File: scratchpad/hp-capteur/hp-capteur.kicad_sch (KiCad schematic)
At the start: 19 parts, among them J1 vers XIAO ESP32-C3, U1 MCP6002

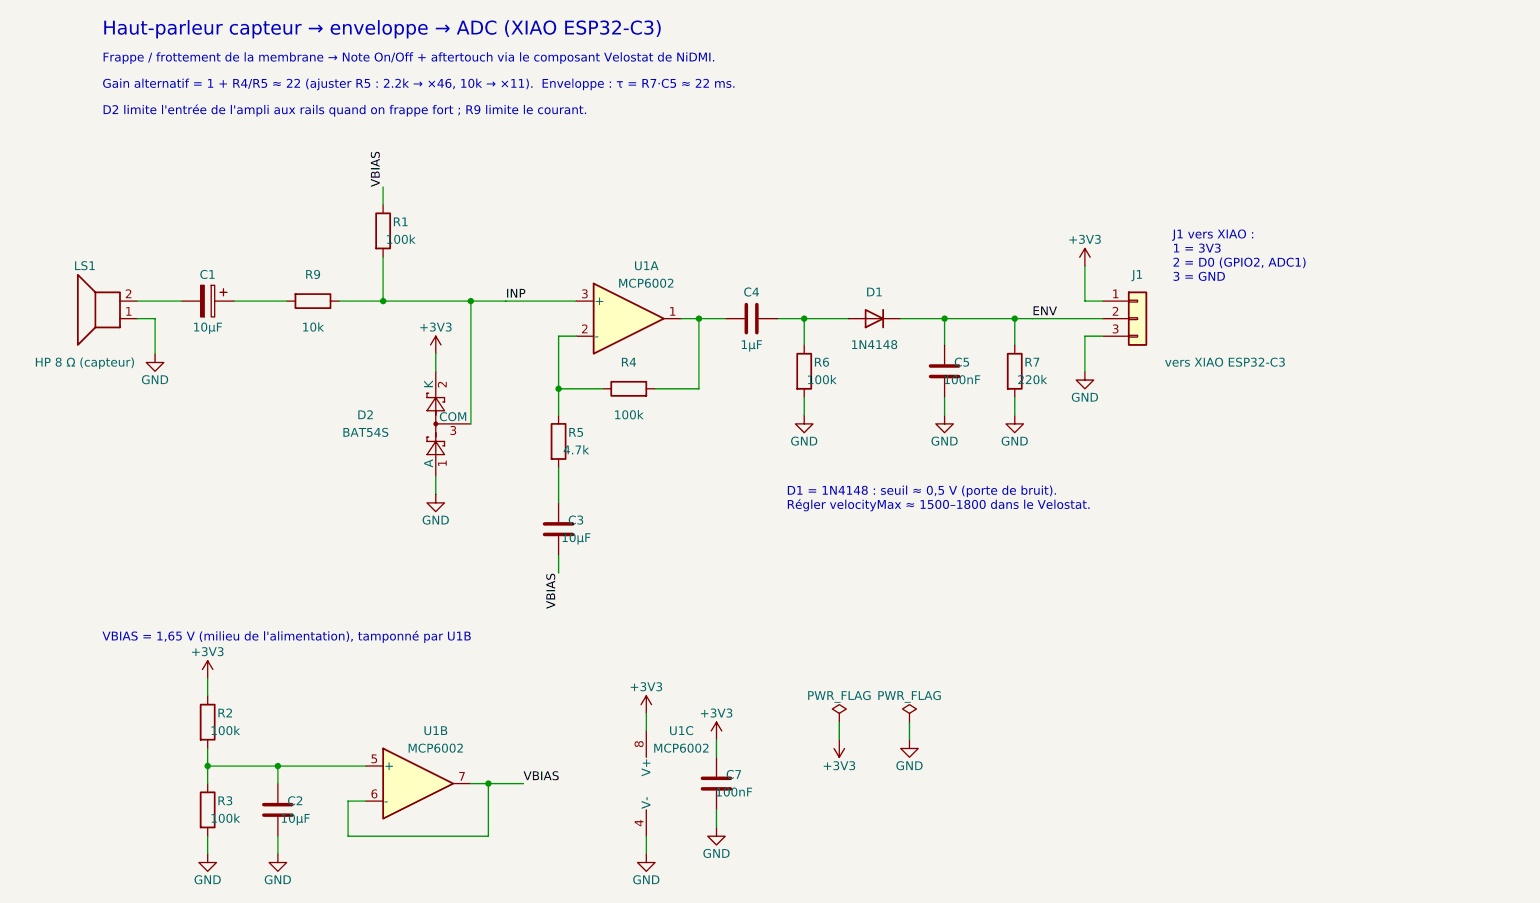
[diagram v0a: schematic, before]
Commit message: Schéma hp-capteur : clamp d'entrée en deux 1N4148 au lieu du BAT54S
D2 (INP → 3V3) et D3 (GND → INP) limitent l'entrée de l'ampli à
−0,6 V / +3,9 V ; R9 (10 k) limite le courant d'injection.

Co-Authored-By: Claude Opus 5.5 <noreply@anthropic.com>
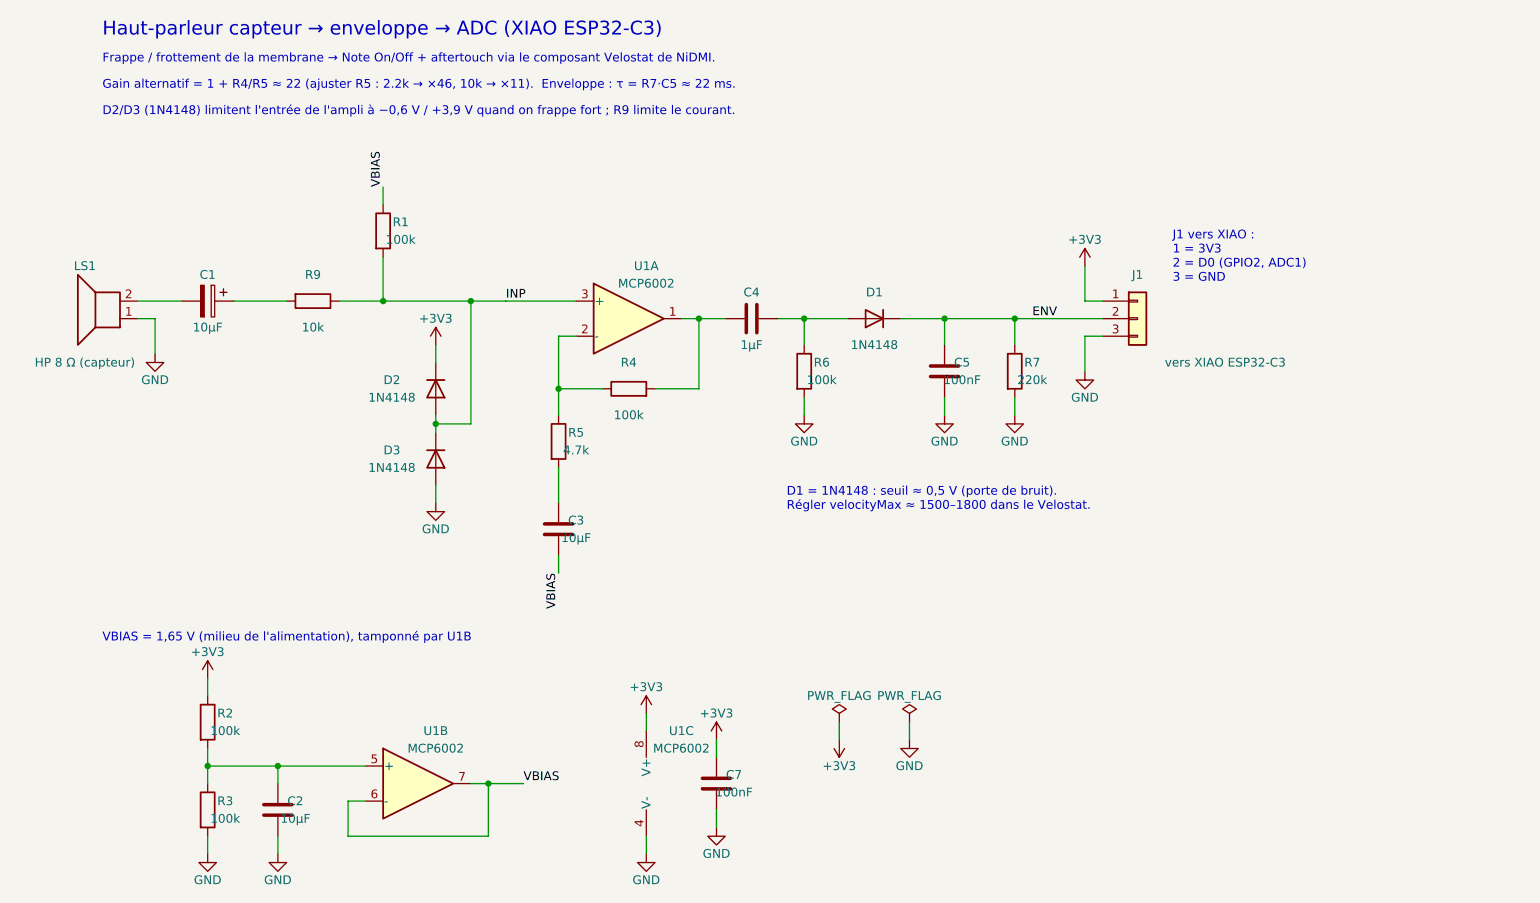
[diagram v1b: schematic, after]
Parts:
- added D3: 1N4148, symbol Diode:1N4148
- D2: value BAT54S -> 1N4148; symbol Diode:BAT54S -> Diode:1N4148
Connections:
- net +3V3: now also D2.1 (K); no longer D2.2 (K)
- net GND: now also D3.2 (A); no longer D2.1 (A)
- net INP: now also D2.2 (A), D3.1 (K); no longer D2.3 (COM)
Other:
- note added: "D2/D3 (1N4148) limitent l'entrée de l'ampli à −0,6 V / +3,9 V quand on frappe fort ; R9 limite le courant."
- note removed: "D2 limite l'entrée de l'ampli aux rails quand on frappe fort ; R9 limite le courant."
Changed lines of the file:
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@@
 	(wire
 		(pts
-			(xy 73.66 81.28)
-			(xy 73.66 83.82)
-		)
-		(stroke
-			(width 0)
-			(type default)
-		)
-	)
-	(wire
-		(pts
-			(xy 73.66 66.04)
-			(xy 73.66 63.5)
+			(xy 73.66 64.77)
+			(xy 73.66 62.23)
+		)
+		(stroke
+			(width 0)
+			(type default)
+		)
+	)
+	(wire
+		(pts
+			(xy 73.66 82.55)
+			(xy 73.66 85.09)
 		)
 		(stroke
@@
 			(xy 66.04 49.53)
 			(xy 66.04 55.88)
+		)
+		(stroke
+			(width 0)
+			(type default)
+		)
+	)
+	(wire
+		(pts
+			(xy 73.66 72.39)
+			(xy 73.66 73.66)
+		)
+		(stroke
+			(width 0)
+			(type default)
+		)
+	)
+	(wire
+		(pts
+			(xy 73.66 73.66)
+			(xy 73.66 74.93)
+		)
+		(stroke
+			(width 0)
+			(type default)
+		)
+	)
+	(wire
+		(pts
+			(xy 73.66 73.66)
+			(xy 78.74 73.66)
 		)
 		(stroke
@@
 	(junction
 		(at 78.74 55.88)
+		(diameter 0)
+		(color 0 0 0 0)
+	)
+	(junction
+		(at 73.66 73.66)
 		(diameter 0)
 		(color 0 0 0 0)
@@
 		)
 	)
-	(text "D2 limite l'entrée de l'ampli aux rails quand on frappe fort ; R9 limite le courant."
+	(text "D2/D3 (1N4148) limitent l'entrée de l'ampli à −0,6 V / +3,9 V quand on frappe fort ; R9 limite le courant."
 		(exclude_from_sim no)
 		(at 25.4 29.21 0)
@@
 	)
 	(symbol
-		(lib_id "Diode:BAT54S")
-		(at 73.66 73.66 90)
+		(lib_id "Diode:1N4148")
+		(at 73.66 68.58 270)
 		(unit 1)
 		(exclude_from_sim no)
@@
 		(dnp no)
 		(property "Reference" "D2"
-			(at 63.5 72.39 90)
-			(effects
-				(font
-					(size 1.27 1.27)
-				)
-			)
-		)
-		(property "Value" "BAT54S"
-			(at 63.5 74.93 90)
+			(at 67.31 67.31 90)
+			(effects
+				(font
+					(size 1.27 1.27)
+				)
+			)
+		)
+		(property "Value" "1N4148"
+			(at 67.31 69.85 90)
 			(effects
 				(font
@@
 		)
 		(property "Footprint" ""
-			(at 73.66 73.66 0)
+			(at 73.66 68.58 0)
 			(effects
 				(font
@@
 		)
 		(property "Datasheet" ""
-			(at 73.66 73.66 0)
+			(at 73.66 68.58 0)
 			(effects
 				(font
@@
 		)
 		(pin "1"
-		)
-		(pin "3"
 		)
 		(pin "2"
@@
 	)
 	(symbol
-		(lib_id "power:GND")
-		(at 73.66 83.82 0)
+		(lib_id "power:+3V3")
+		(at 73.66 62.23 0)
 		(unit 1)
 		(exclude_from_sim no)
@@
 		(dnp no)
 		(property "Reference" "#PWR001"
-			(at 73.66 83.82 0)
-			(effects
-				(font
-					(size 1.27 1.27)
-				)
-				(hide yes)
-			)
-		)
-		(property "Value" "GND"
-			(at 73.66 87.63 0)
+			(at 73.66 62.23 0)
+			(effects
+				(font
+					(size 1.27 1.27)
+				)
+				(hide yes)
+			)
+		)
+		(property "Value" "+3V3"
+			(at 73.66 58.42 0)
 			(effects
 				(font
@@
 		)
 		(property "Footprint" ""
-			(at 73.66 83.82 0)
+			(at 73.66 62.23 0)
 			(effects
 				(font
@@
 		)
 		(property "Datasheet" ""
-			(at 73.66 83.82 0)
+			(at 73.66 62.23 0)
 			(effects
 				(font
@@
 	)
 	(symbol
-		(lib_id "power:+3V3")
-		(at 73.66 63.5 0)
+		(lib_id "Diode:1N4148")
+		(at 73.66 78.74 270)
+		(unit 1)
+		(exclude_from_sim no)
+		(in_bom yes)
+		(on_board yes)
+		(dnp no)
+		(property "Reference" "D3"
+			(at 67.31 77.47 90)
+			(effects
+				(font
+					(size 1.27 1.27)
+				)
+			)
+		)
+		(property "Value" "1N4148"
+			(at 67.31 80.01 90)
+			(effects
+				(font
+					(size 1.27 1.27)
+				)
+			)
+		)
+		(property "Footprint" ""
+			(at 73.66 78.74 0)
+			(effects
+				(font
+					(size 1.27 1.27)
+				)
+				(hide yes)
+			)
+		)
+		(property "Datasheet" ""
+			(at 73.66 78.74 0)
+			(effects
+				(font
+					(size 1.27 1.27)
+				)
+				(hide yes)
+			)
+		)
+		(pin "1"
+		)
+		(pin "2"
+		)
+		(instances
+			(project "hp-capteur"
+				(path "/462643ff-c9af-55b7-87ee-4acf96ab3226"
+					(reference "D3")
+					(unit 1)
+				)
+			)
+		)
+	)
+	(symbol
+		(lib_id "power:GND")
+		(at 73.66 85.09 0)
 		(unit 1)
 		(exclude_from_sim no)
@@
 		(dnp no)
 		(property "Reference" "#PWR002"
-			(at 73.66 63.5 0)
-			(effects
-				(font
-					(size 1.27 1.27)
-				)
-				(hide yes)
-			)
-		)
-		(property "Value" "+3V3"
-			(at 73.66 59.69 0)
+			(at 73.66 85.09 0)
+			(effects
+				(font
+					(size 1.27 1.27)
+				)
+				(hide yes)
+			)
+		)
+		(property "Value" "GND"
+			(at 73.66 88.9 0)
 			(effects
 				(font
@@
 		)
 		(property "Footprint" ""
-			(at 73.66 63.5 0)
+			(at 73.66 85.09 0)
 			(effects
 				(font
@@
 		)
 		(property "Datasheet" ""
-			(at 73.66 63.5 0)
-			(effects
-				(font
+			(at 73.66 85.09 0)
+			(effects
+				(font

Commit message: Schéma hp-capteur : deux voies, frappes (enveloppe) et frottement (RMS)
- J1 à 4 broches : ENV → D0 (GPIO2) pour le Velostat, AMP → D1 (GPIO3)
  pour un RMS logiciel (aftertouch du frottement léger, sans zone morte).
- VBIAS à 1,25 V (R2 160k) : la sortie du préampli couvre la plage ADC 0–2,5 V.
- Gain ≈ 46 (R5 2.2k) ; R6 10k pour limiter la dérive de C4 en signal continu.

Co-Authored-By: Claude Opus 5.5 <noreply@anthropic.com>
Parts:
- J1: symbol Connector_Generic:Conn_01x03 -> Connector_Generic:Conn_01x04
- R2: value 100k -> 160k
- R5: value 4.7k -> 2.2k
- R6: value 100k -> 10k
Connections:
- net GND: now also J1.4 (Pin_4); no longer J1.3 (Pin_3)
- net AMP: now reaches C4.1, R4.2, U1.1
- net AMP: now also J1.3 (Pin_3)
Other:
- note added: "Deux voies : ENV (enveloppe analogique) pour les frappes → Velostat ; AMP (préampli brut) pour le frottement → RMS logiciel → aftertouch."
- note added: "Frappe de la membrane → Note On/Off + vélocité ; frottement → aftertouch (composants NiDMI)."
- note added: "Gain alternatif = 1 + R4/R5 ≈ 46 (ajuster R5 : 1k → ×100, 4.7k → ×22). Enveloppe : τ = R7·C5 ≈ 22 ms."
- note added: "J1 vers XIAO : 1 = 3V3 2 = ENV → broche D0 (GPIO2) : frappes 3 = AMP → broche D1 (GPIO3) : frottement 4 = GND"
- note added: "VBIAS = 1,25 V (milieu de la plage ADC 0–2,5 V), tamponné par U1B"
- note removed: "Frappe / frottement de la membrane → Note On/Off + aftertouch via le composant Velostat de NiDMI."
- note removed: "Gain alternatif = 1 + R4/R5 ≈ 22 (ajuster R5 : 2.2k → ×46, 10k → ×11). Enveloppe : τ = R7·C5 ≈ 22 ms."
- note removed: "J1 vers XIAO : 1 = 3V3 2 = D0 (GPIO2, ADC1) 3 = GND"
- note removed: "VBIAS = 1,65 V (milieu de l'alimentation), tamponné par U1B"
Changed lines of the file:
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@@
 		(title "Haut-parleur capteur → XIAO ESP32-C3")
 		(date "2026-10-15")
-		(rev "0.1")
+		(rev "0.2")
 		(company "NiDMI")
-		(comment 1 "Enveloppe pour le composant Velostat (Note On/Off + aftertouch)")
+		(comment 1 "Deux voies : frappes (enveloppe → Velostat) + frottement (RMS logiciel → aftertouch)")
 	)
 	(label "VBIAS"
@@
 		)
 	)
+	(label "AMP"
+		(at 167.64 60.96 180)
+		(fields_autoplaced yes)
+		(effects
+			(font
+				(size 1.27 1.27)
+			)
+			(justify right bottom)
+		)
+	)
 	(wire
 		(pts
@@
 	(wire
 		(pts
+			(xy 170.18 60.96)
+			(xy 167.64 60.96)
+		)
+		(stroke
+			(width 0)
+			(type default)
+		)
+	)
+	(wire
+		(pts
 			(xy 40.64 113.03)
 			(xy 40.64 110.49)
@@
 		(pts
 			(xy 111.76 68.58)
+			(xy 111.76 63.5)
+		)
+		(stroke
+			(width 0)
+			(type default)
+		)
+	)
+	(wire
+		(pts
+			(xy 111.76 63.5)
 			(xy 111.76 58.42)
 		)
@@
 	(wire
 		(pts
-			(xy 170.18 60.96)
-			(xy 167.64 60.96)
-		)
-		(stroke
-			(width 0)
-			(type default)
-		)
-	)
-	(wire
-		(pts
-			(xy 167.64 60.96)
-			(xy 167.64 66.04)
+			(xy 170.18 63.5)
+			(xy 165.1 63.5)
+		)
+		(stroke
+			(width 0)
+			(type default)
+		)
+	)
+	(wire
+		(pts
+			(xy 165.1 63.5)
+			(xy 165.1 68.58)
 		)
 		(stroke
@@
 		)
 	)
+	(label "AMP"
+		(at 111.76 63.5 0)
+		(fields_autoplaced yes)
+		(effects
+			(font
+				(size 1.27 1.27)
+			)
+			(justify left bottom)
+		)
+	)
 	(wire
 		(pts
@@
 		)
 	)
-	(text "Frappe / frottement de la membrane → Note On/Off + aftertouch via le composant Velostat de NiDMI."
+	(text "Frappe de la membrane → Note On/Off + vélocité ; frottement → aftertouch (composants NiDMI)."
 		(exclude_from_sim no)
 		(at 25.4 21.59 0)
@@
 		)
 	)
-	(text "Gain alternatif = 1 + R4/R5 ≈ 22 (ajuster R5 : 2.2k → ×46, 10k → ×11).  Enveloppe : τ = R7·C5 ≈ 22 ms."
+	(text "Gain alternatif = 1 + R4/R5 ≈ 46 (ajuster R5 : 1k → ×100, 4.7k → ×22).  Enveloppe : τ = R7·C5 ≈ 22 ms."
 		(exclude_from_sim no)
 		(at 25.4 25.4 0)
@@
 		)
 	)
+	(text "Deux voies : ENV (enveloppe analogique) pour les frappes → Velostat ; AMP (préampli brut) pour le frottement → RMS logiciel → aftertouch."
+		(exclude_from_sim no)
+		(at 25.4 33.02 0)
+		(effects
+			(font
+				(size 1.27 1.27)
+			)
+			(justify left bottom)
+		)
+	)
 	(text "D2/D3 (1N4148) limitent l'entrée de l'ampli à −0,6 V / +3,9 V quand on frappe fort ; R9 limite le courant."
 		(exclude_from_sim no)
@@
 		)
 	)
-	(text "VBIAS = 1,65 V (milieu de l'alimentation), tamponné par U1B"
+	(text "VBIAS = 1,25 V (milieu de la plage ADC 0–2,5 V), tamponné par U1B"
 		(exclude_from_sim no)
 		(at 25.4 105.41 0)
@@
 		)
 	)
-	(text "J1 vers XIAO :\n1 = 3V3\n2 = D0 (GPIO2, ADC1)\n3 = GND"
+	(text "J1 vers XIAO :\n1 = 3V3\n2 = ENV → broche D0 (GPIO2) : frappes\n3 = AMP → broche D1 (GPIO3) : frottement\n4 = GND"
 		(exclude_from_sim no)
 		(at 180.34 53.34 0)
@@
 			)
 		)
-		(property "Value" "4.7k"
+		(property "Value" "2.2k"
 			(at 93.98 77.47 0)
 			(effects
@@
 			)
 		)
-		(property "Value" "100k"
+		(property "Value" "10k"
 			(at 129.54 67.31 0)
 			(effects
@@
 	)
 	(symbol
-		(lib_id "Connector_Generic:Conn_01x03")
+		(lib_id "Connector_Generic:Conn_01x04")
 		(at 175.26 58.42 0)
 		(unit 1)
@@
 		)
 		(property "Value" "vers XIAO ESP32-C3"
-			(at 187.96 64.77 0)
+			(at 175.26 64.77 0)
 			(effects
 				(font
@@
 		)
 		(pin "3"
+		)
+		(pin "4"
 		)
 		(instances
@@
 			)
 		)
-		(property "Value" "100k"
+		(property "Value" "160k"
 			(at 43.18 118.11 0)
 			(effects
@@
 	(symbol
 		(lib_id "power:GND")
-		(at 167.64 66.04 0)
+		(at 165.1 68.58 0)
 		(unit 1)
 		(exclude_from_sim no)
@@
 		(dnp no)
 		(property "Reference" "#PWR015"
-			(at 167.64 66.04 0)
+			(at 165.1 68.58 0)
 			(effects
 				(font
@@
 		)
 		(property "Value" "GND"
-			(at 167.64 69.85 0)
-			(effects
-				(font
-					(size 1.27 1.27)
-				)
-			)
-		)
-		(property "Footprint" ""
-			(at 167.64 66.04 0)
-			(effects
-				(font
-					(size 1.27 1.27)
-				)
-				(hide yes)
-			)
-		)
-		(property "Datasheet" ""
-			(at 167.64 66.04 0)
-			(effects
-				(font
+			(at 165.1 72.39 0)
+			(effects
+				(font
+					(size 1.27 1.27)
+				)
+			)
+		)
+		(property "Footprint" ""
+			(at 165.1 68.58 0)
+			(effects
+				(font
+					(size 1.27 1.27)
+				)
+				(hide yes)
+			)
+		)
+		(property "Datasheet" ""
+			(at 165.1 68.58 0)
+			(effects
+				(font
